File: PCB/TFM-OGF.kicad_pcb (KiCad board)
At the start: 2 copper layers, 74 x 74 mm, 27 parts, among them J1 Alimentación, J10 5V Output, J11 3.3V Output, J2 CAN_Externo, J3 Jumper CAN, J4 Jumper CAN, J5 Lado izquierdo, J6 Lado derecho, J7 Lado izquierdo, J8 Lado derecho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

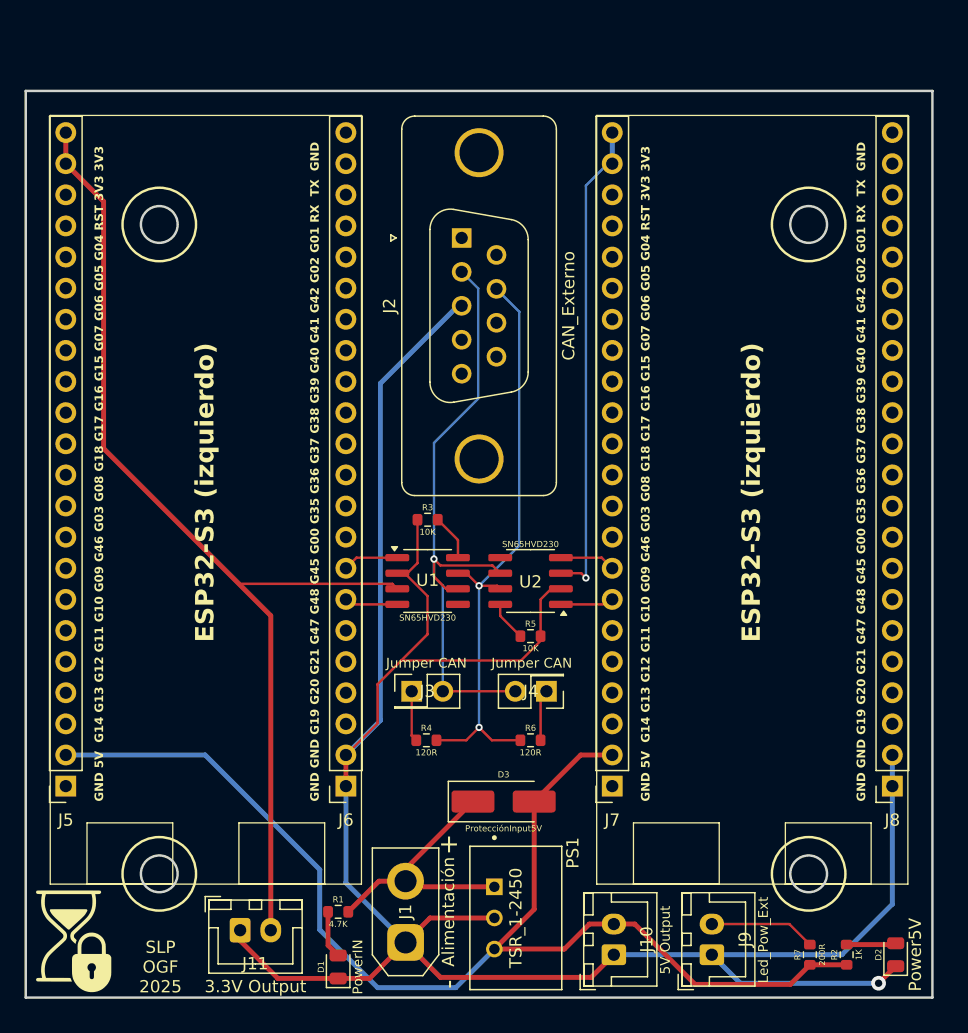
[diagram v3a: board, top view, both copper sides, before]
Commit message: Amplío la placa 0.8mm a la derecha
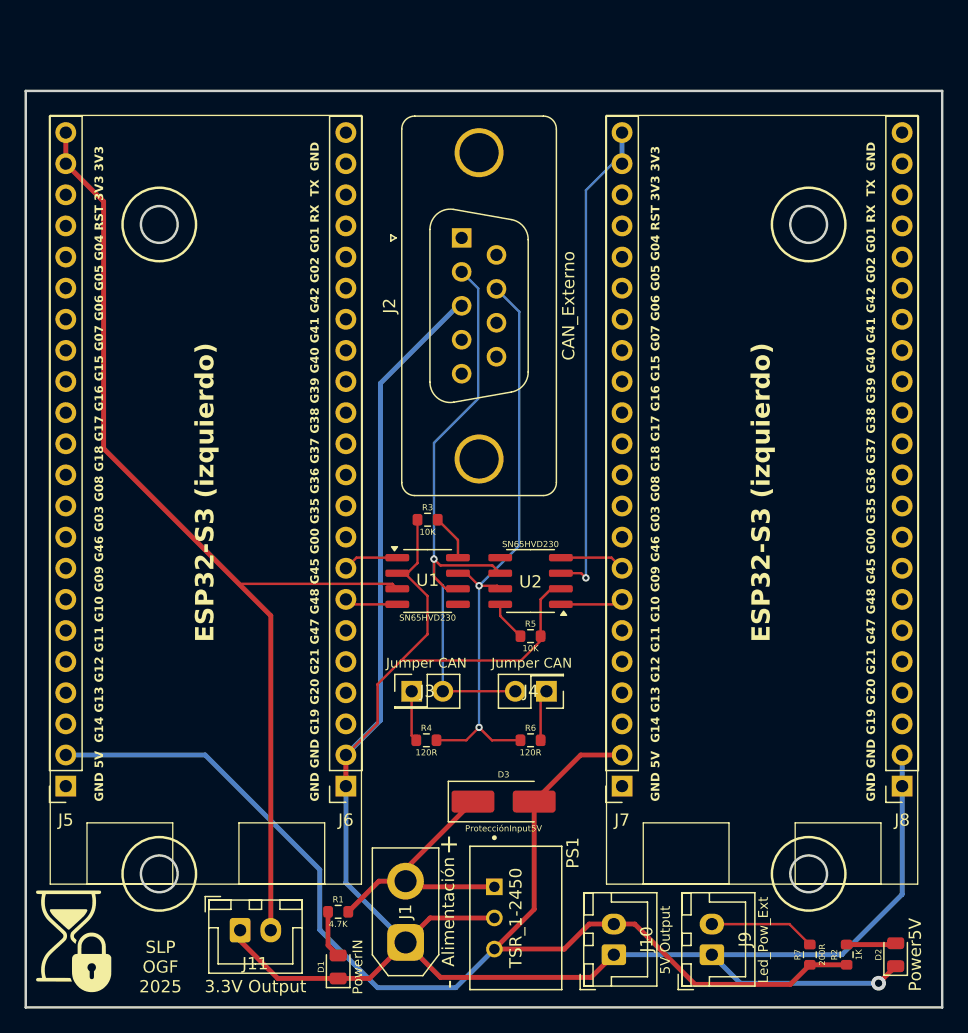
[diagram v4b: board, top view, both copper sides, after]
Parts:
- moved G1 1.00 mm to (136.0, 146.0)
- moved J8 0.80 mm to (171.5, 156.7)
- moved J7 0.80 mm to (148.7, 156.7)
- moved G3 0.50 mm to (137.5, 113.0)
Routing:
- net RxCANDer_G09_2: track 4.55 -> 5.35 mm
- net TxCANDer_G10_2: track 4.36 -> 5.16 mm
- net 5V: track 100.7 -> 101.5 mm
- net 3.3V_2: track 39.7 -> 40.2 mm
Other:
- board size 74 x 74 mm -> 74.8 x 74.8 mm
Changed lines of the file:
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@@
 	(title_block
 		(title "TFM-OGF")
-		(date "2025-05-12")
+		(date "2025-05-13")
 		(rev "1.0")
 		(company "UNIR")
@@
 			(psa4output no)
 			(plot_black_and_white yes)
+			(plotinvisibletext no)
 			(sketchpadsonfab no)
 			(plotpadnumbers no)
@@
 	(footprint "Connector_PinSocket_2.54mm:PinSocket_1x22_P2.54mm_Vertical"
 		(layer "F.Cu")
-		(at 147.87 156.74 180)
+		(at 148.67 156.74 180)
 		(descr "Through hole straight socket strip, 1x22, 2.54mm pitch, single row (from Kicad 4.0.7), script generated")
 		(tags "Through hole socket strip THT 1x22 2.54mm single row")
@@
 	(footprint "Connector_PinSocket_2.54mm:PinSocket_1x22_P2.54mm_Vertical"
 		(layer "F.Cu")
-		(at 170.73 156.74 180)
+		(at 171.53 156.74 180)
 		(descr "Through hole straight socket strip, 1x22, 2.54mm pitch, single row (from Kicad 4.0.7), script generated")
 		(tags "Through hole socket strip THT 1x22 2.54mm single row")
@@
 	(footprint "LOGO"
 		(layer "B.Cu")
-		(at 135 146 180)
+		(at 136 146 180)
 		(property "Reference" "G1"
 			(at 0 0 0)
@@
 	(footprint "LOGO"
 		(layer "B.Cu")
-		(at 137 113 180)
+		(at 137.5 113 180)
 		(property "Reference" "G3"
 			(at 0 0 0)
@@
 	)
 	(gr_rect
-		(start 146.6 102)
-		(end 172 164.74)
+		(start 147.4 102)
+		(end 172.8 164.74)
 		(stroke
 			(width 0.1)
@@
 	)
 	(gr_rect
-		(start 162 159.74)
-		(end 169 164.74)
+		(start 162.8 159.74)
+		(end 169.8 164.74)
 		(stroke
 			(width 0.1)
@@
 	)
 	(gr_rect
-		(start 149.6 159.74)
-		(end 156.6 164.74)
+		(start 150.4 159.74)
+		(end 157.4 164.74)
 		(stroke
 			(width 0.1)
@@
 	(gr_rect
 		(start 100 100)
-		(end 174 174)
+		(end 174.8 174.8)
 		(stroke
 			(width 0.2)
@@
 	)
 	(gr_text "GND GND G19 G20 G21 G47 G48 G45 G00 G35 G36 G37 G38 G39 G40 G41 G42 G02 G01 RX  TX  GND"
-		(at 168.6 158 90)
+		(at 169.4 158 90)
 		(layer "F.SilkS")
 		(effects
@@
 	)
 	(gr_text "ESP32-S3 (izquierdo)"
-		(at 160.1 145 90)
+		(at 160.9 145 90)
 		(layer "F.SilkS")
 		(effects
@@
 	)
 	(gr_text "GND 5V  G14 G13 G12 G11 G10 G09 G46 G03 G08 G18 G17 G16 G15 G07 G06 G05 G04 RST 3V3 3V3"
-		(at 151 158 90)
+		(at 151.8 158 90)
 		(layer "F.SilkS")
 		(effects
@@
 	)
 	(segment
+		(start 171.53 156.74)
+		(end 171.53 165.58)
+		(width 0.4)
+		(layer "B.Cu")
+		(net 1)
+	)
+	(segment
+		(start 171.53 165.58)
+		(end 166.61 170.5)
+		(width 0.4)
+		(layer "B.Cu")
+		(net 1)
+	)
+	(segment
 		(start 126.13 164.63)
 		(end 126.13 156.74)
@@
 	)
 	(segment
-		(start 170.73 156.74)
-		(end 170.73 166.38)
-		(width 0.4)
-		(layer "B.Cu")
-		(net 1)
-	)
-	(segment
 		(start 131 169.5)
 		(end 126.13 164.63)
@@
 	)
 	(segment
-		(start 170.73 166.38)
-		(end 166.61 170.5)
-		(width 0.4)
-		(layer "B.Cu")
-		(net 1)
-	)
-	(segment
-		(start 170.73 156.74)
-		(end 170.73 154.2)
+		(start 171.53 156.74)
+		(end 171.53 154.2)
 		(width 0.4)
 		(layer "B.Cu")
@@
 	)
 	(segment
-		(start 148 170.5)
+		(start 166.61 170.5)
 		(end 156 170.5)
 		(width 0.4)
@@
 	)
 	(segment
-		(start 166.61 170.5)
+		(start 148 170.5)
 		(end 156 170.5)
 		(width 0.4)
@@
 	)
 	(segment
-		(start 147.87 154.2)
-		(end 145.3 154.2)
+		(start 148 168)
+		(end 149.71 168)
 		(width 0.4)
 		(layer "F.Cu")
@@
 	)
 	(segment
-		(start 148 168)
-		(end 149.71 168)
+		(start 145.3 154.2)
+		(end 141.5 158)
 		(width 0.4)
 		(layer "F.Cu")
@@
 	)
 	(segment
+		(start 148.67 154.2)
+		(end 145.3 154.2)
+		(width 0.4)
+		(layer "F.Cu")
+		(net 4)
+	)
+	(segment
 		(start 154.63 172.92)
 		(end 162.405 172.92)
@@
 	)
 	(segment
-		(start 145.3 154.2)
-		(end 141.5 158)
-		(width 0.4)
-		(layer "F.Cu")
-		(net 4)
-	)
-	(segment
 		(start 138.25 170.04)
 		(end 143.96 170.04)
@@
 	)
 	(segment
-		(start 147.500559 105.94)
-		(end 147.87 105.94)
-		(width 0.4)
+		(start 145.72 139.75)
+		(end 145.72 108.11)
+		(width 0.2)
 		(layer "B.Cu")
 		(net 24)
 	)
 	(segment
-		(start 147.87 105.94)
-		(end 147.87 103.4)
-		(width 0.4)
+		(start 145.72 108.11)
+		(end 147.89 105.94)
+		(width 0.2)
 		(layer "B.Cu")
 		(net 24)
 	)
 	(segment
-		(start 145.72 107.720559)
-		(end 147.500559 105.94)
+		(start 147.89 105.94)
+		(end 148.67 105.94)
 		(width 0.2)
 		(layer "B.Cu")
@@
 	)
 	(segment
-		(start 145.72 139.75)
-		(end 145.72 107.720559)
-		(width 0.2)
+		(start 148.67 105.94)
+		(end 148.67 103.4)
+		(width 0.4)
 		(layer "B.Cu")
 		(net 24)
@@
 	(segment
 		(start 143.675 141.905)
-		(end 147.465 141.905)
+		(end 148.265 141.905)
 		(width 0.2)
 		(layer "F.Cu")
@@
 	)
 	(segment
-		(start 147.465 141.905)
-		(end 147.87 141.5)
+		(start 148.265 141.905)
+		(end 148.67 141.5)
 		(width 0.2)
 		(layer "F.Cu")
@@
 	)
 	(segment
-		(start 147.005 138.095)
-		(end 143.675 138.095)
+		(start 148.67 138.96)
+		(end 147.805 138.095)
 		(width 0.2)
 		(layer "F.Cu")
@@
 	)
 	(segment
-		(start 147.87 138.96)
-		(end 147.005 138.095)
+		(start 147.805 138.095)
+		(end 143.675 138.095)
 		(width 0.2)
 		(layer "F.Cu")

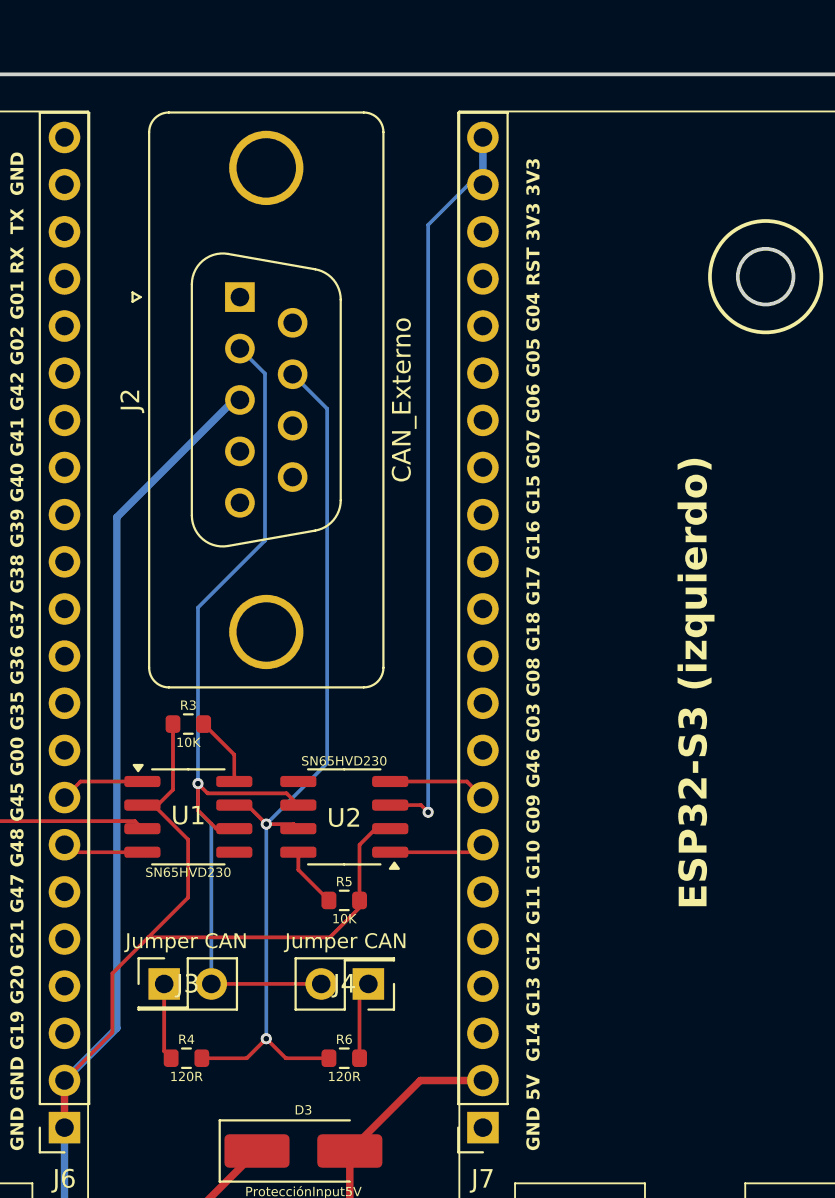
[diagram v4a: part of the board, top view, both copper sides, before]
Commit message: Centro los componentes del medio al haber aumentado 0,8mm a la derecha
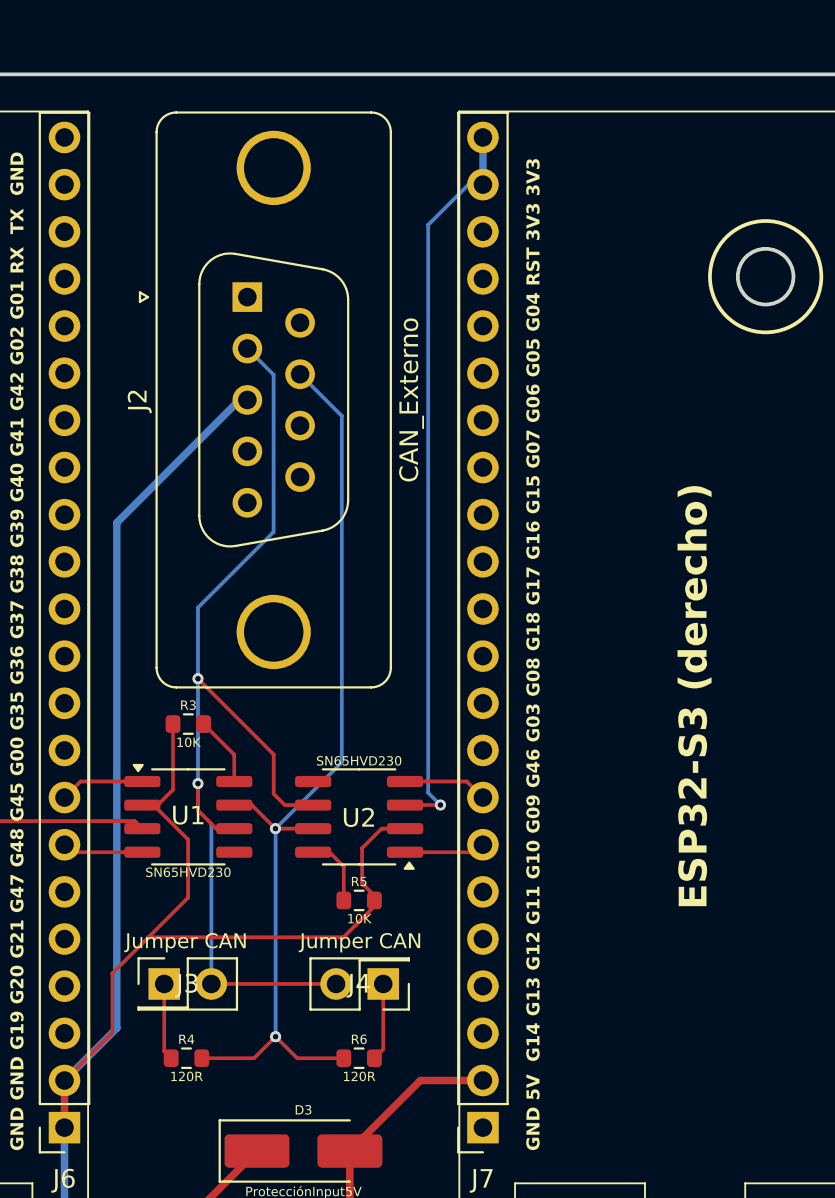
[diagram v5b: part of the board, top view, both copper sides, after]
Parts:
- moved J4 0.80 mm to (143.3, 149.0)
- moved R5 0.80 mm to (142.0, 144.5)
- moved R6 0.80 mm to (142.0, 153.0)
- moved U2 0.80 mm to (142.0, 140.0)
- moved J2 0.40 mm to (136.0, 112.0)
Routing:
- net CAN_Low: track 52.2 -> 57.6 mm, vias 1 -> 2
- net CAN_High: track 49.6 -> 51.5 mm
- net GND: track 197.1 -> 199.0 mm
- net 3.3V_2: track 40.2 -> 39.0 mm
- net TxCANDer_G10_2: track 5.16 -> 4.36 mm
- net RxCANDer_G09_2: track 5.35 -> 4.55 mm
- net Net-(U2-Rs): track 3.28 -> 3.79 mm
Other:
- board text added: "ESP32-S3 (derecho)"

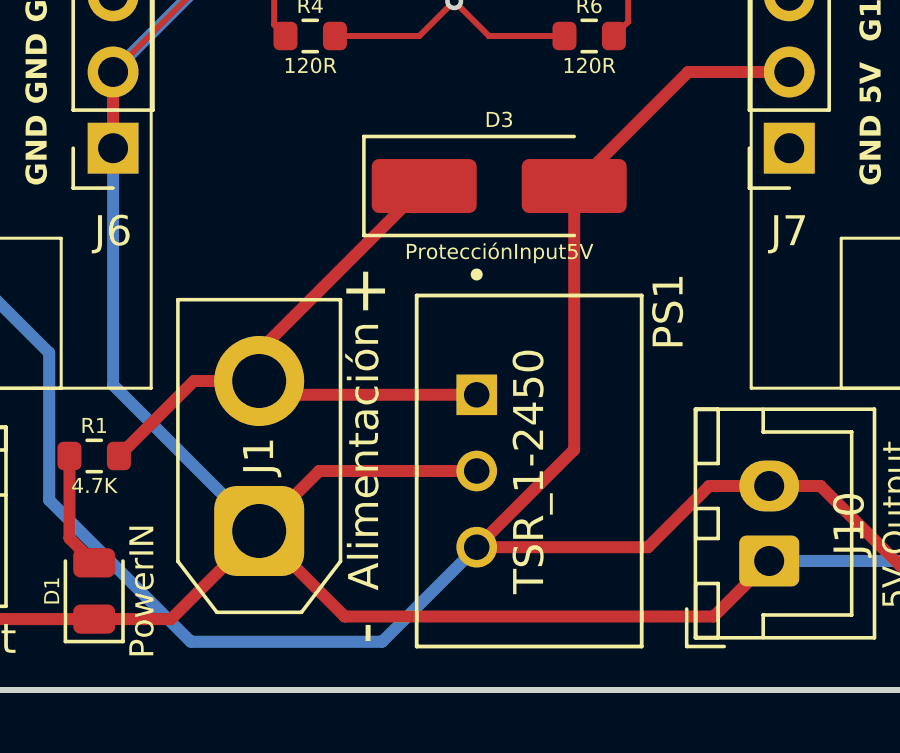
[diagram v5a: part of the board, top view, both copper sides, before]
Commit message: Cambio símbolo y huella TSR1 para usar los de KiCad, regenero ficheros de producción
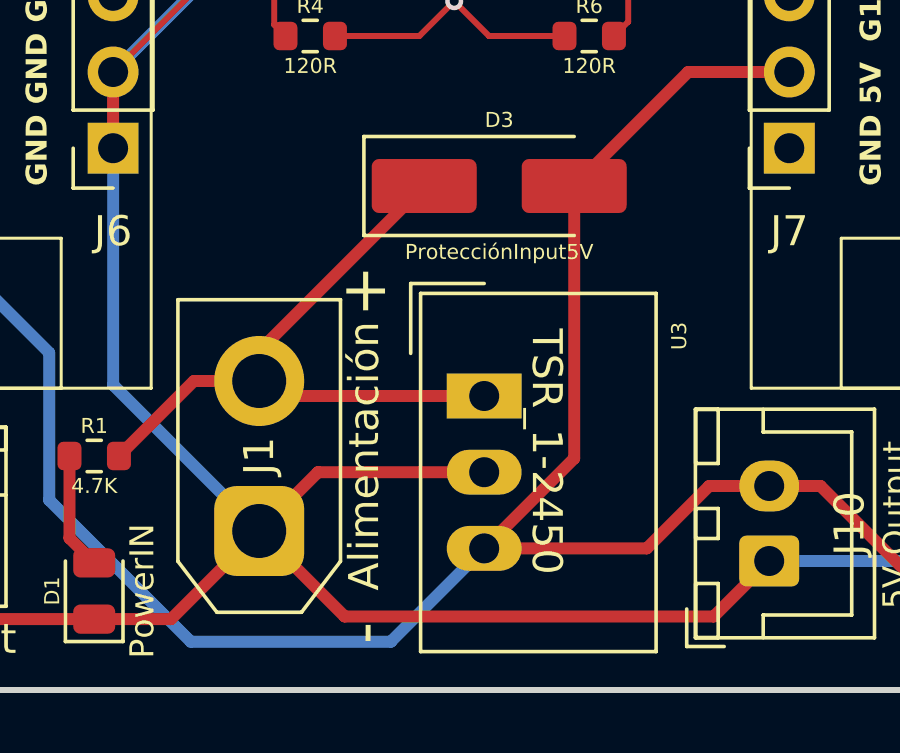
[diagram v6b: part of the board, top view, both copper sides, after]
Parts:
- removed PS1: TSR_1-2450, TSR_1-2450:CONV_TSR_1-2450
- added U3: TSR_1-2450, Converter_DCDC:Converter_DCDC_TRACO_TSR-1_THT, F.Cu at (138.5, 165.0)
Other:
- board text added: "TSR_1-2450"
